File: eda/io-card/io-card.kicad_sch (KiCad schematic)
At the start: 22 parts, among them J3 PortA, J4 PortB, J5 ControlLines, J6 SPI, U1 W65C22SxP, U13 74HCT138, U2 W65C22SxP, U3 74HCT14, U5 74HCT00

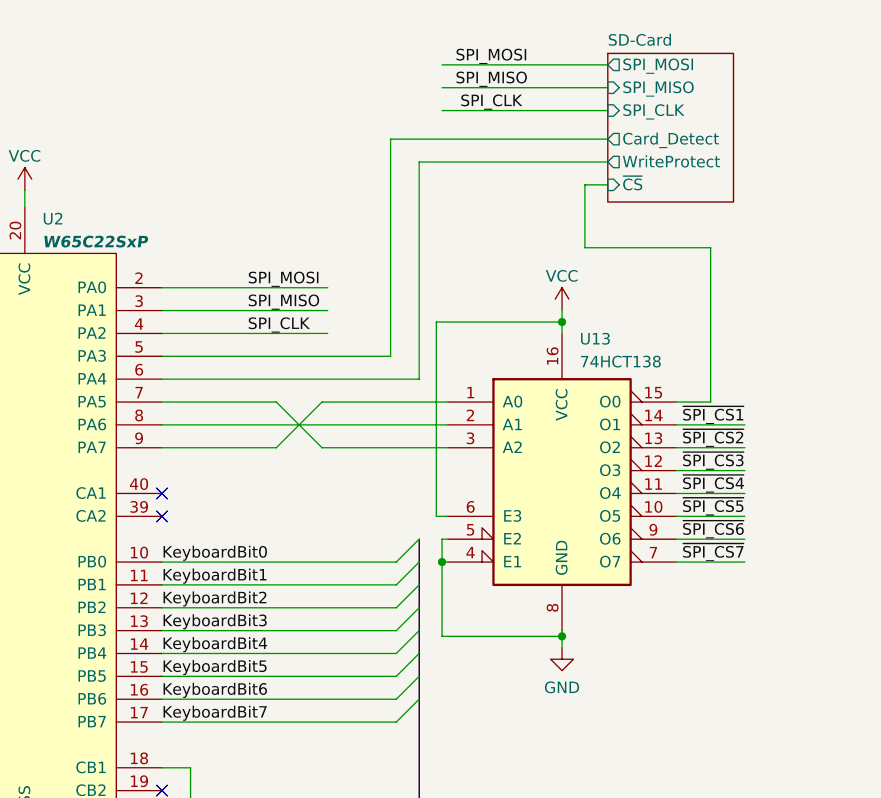
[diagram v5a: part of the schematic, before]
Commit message: Work on SPI with actual hardware
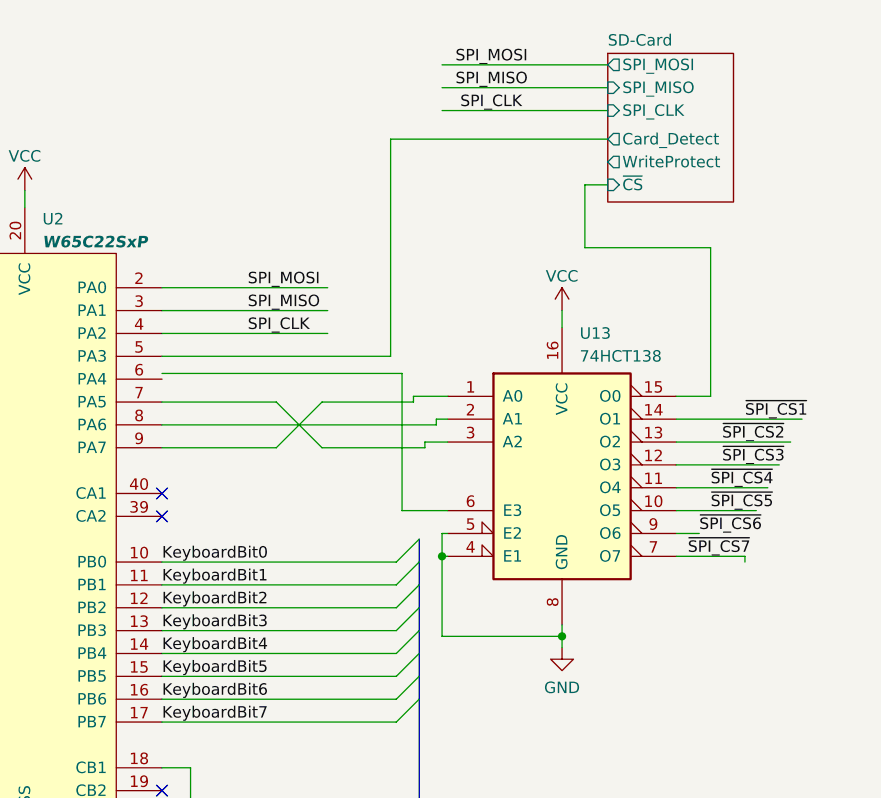
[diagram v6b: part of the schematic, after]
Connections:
- net SD-Card/WriteProtect: no longer U2.6 (PA4)
- net VCC: no longer U13.6 (E3)
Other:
- moved on the sheet: U13

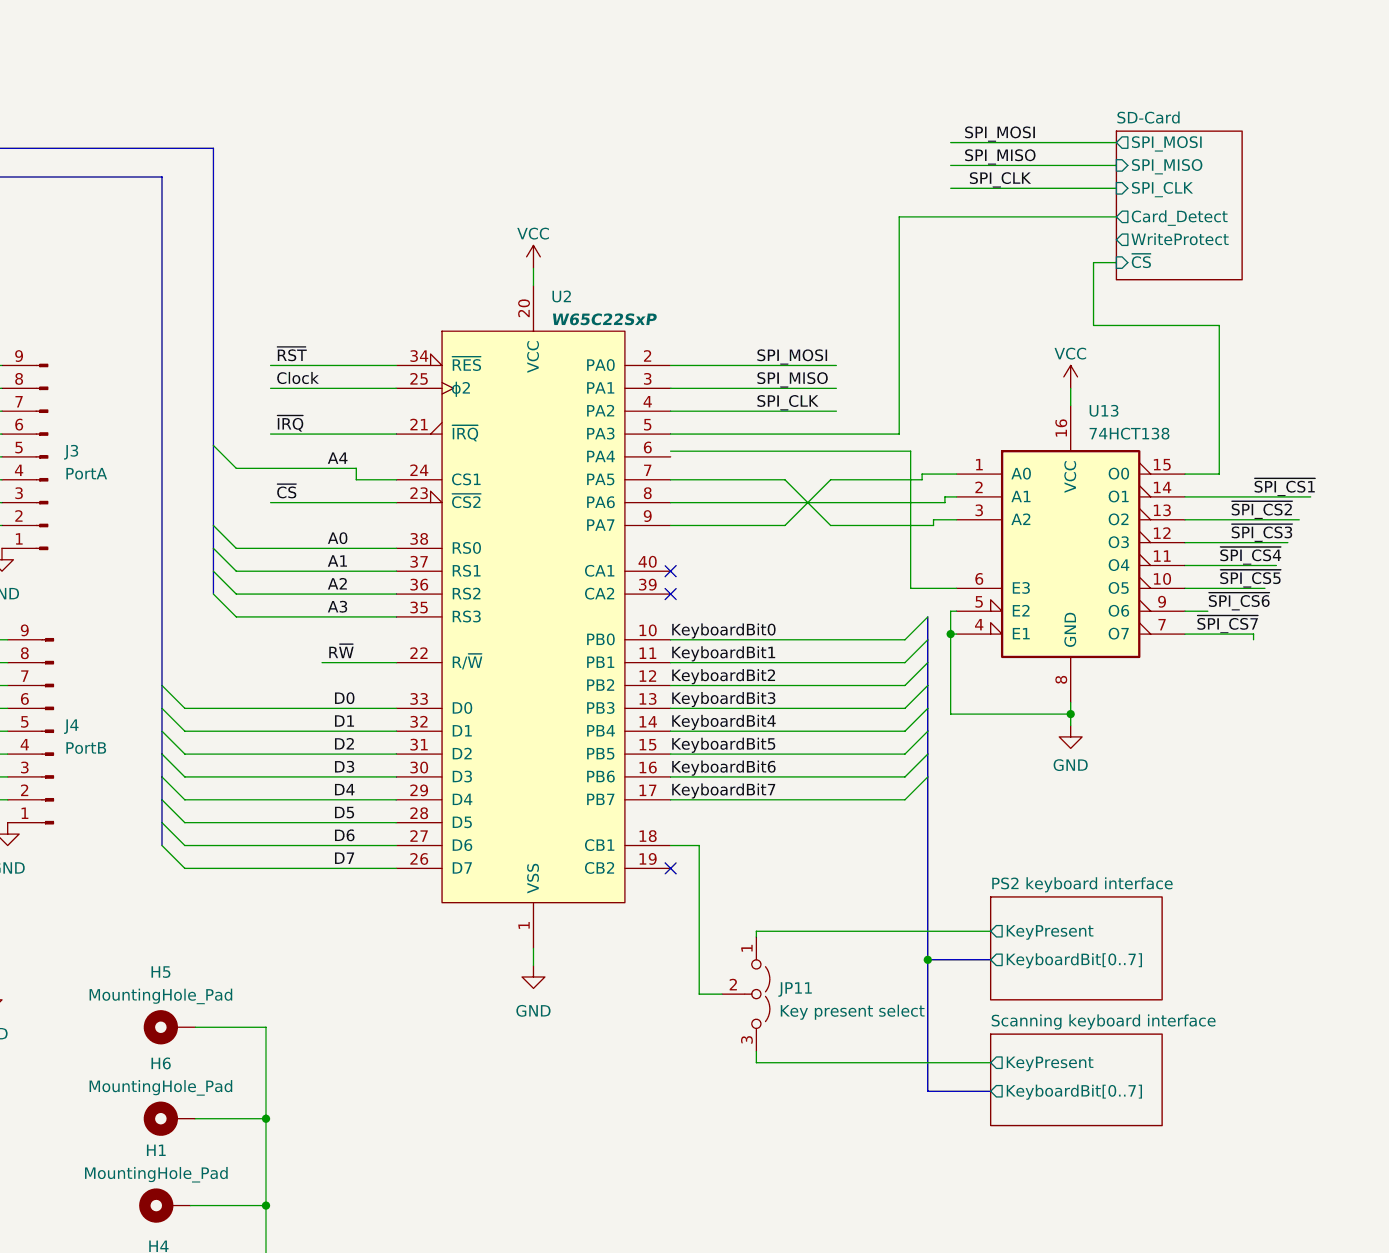
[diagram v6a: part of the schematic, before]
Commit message: Update simulator to match new io card via assignment
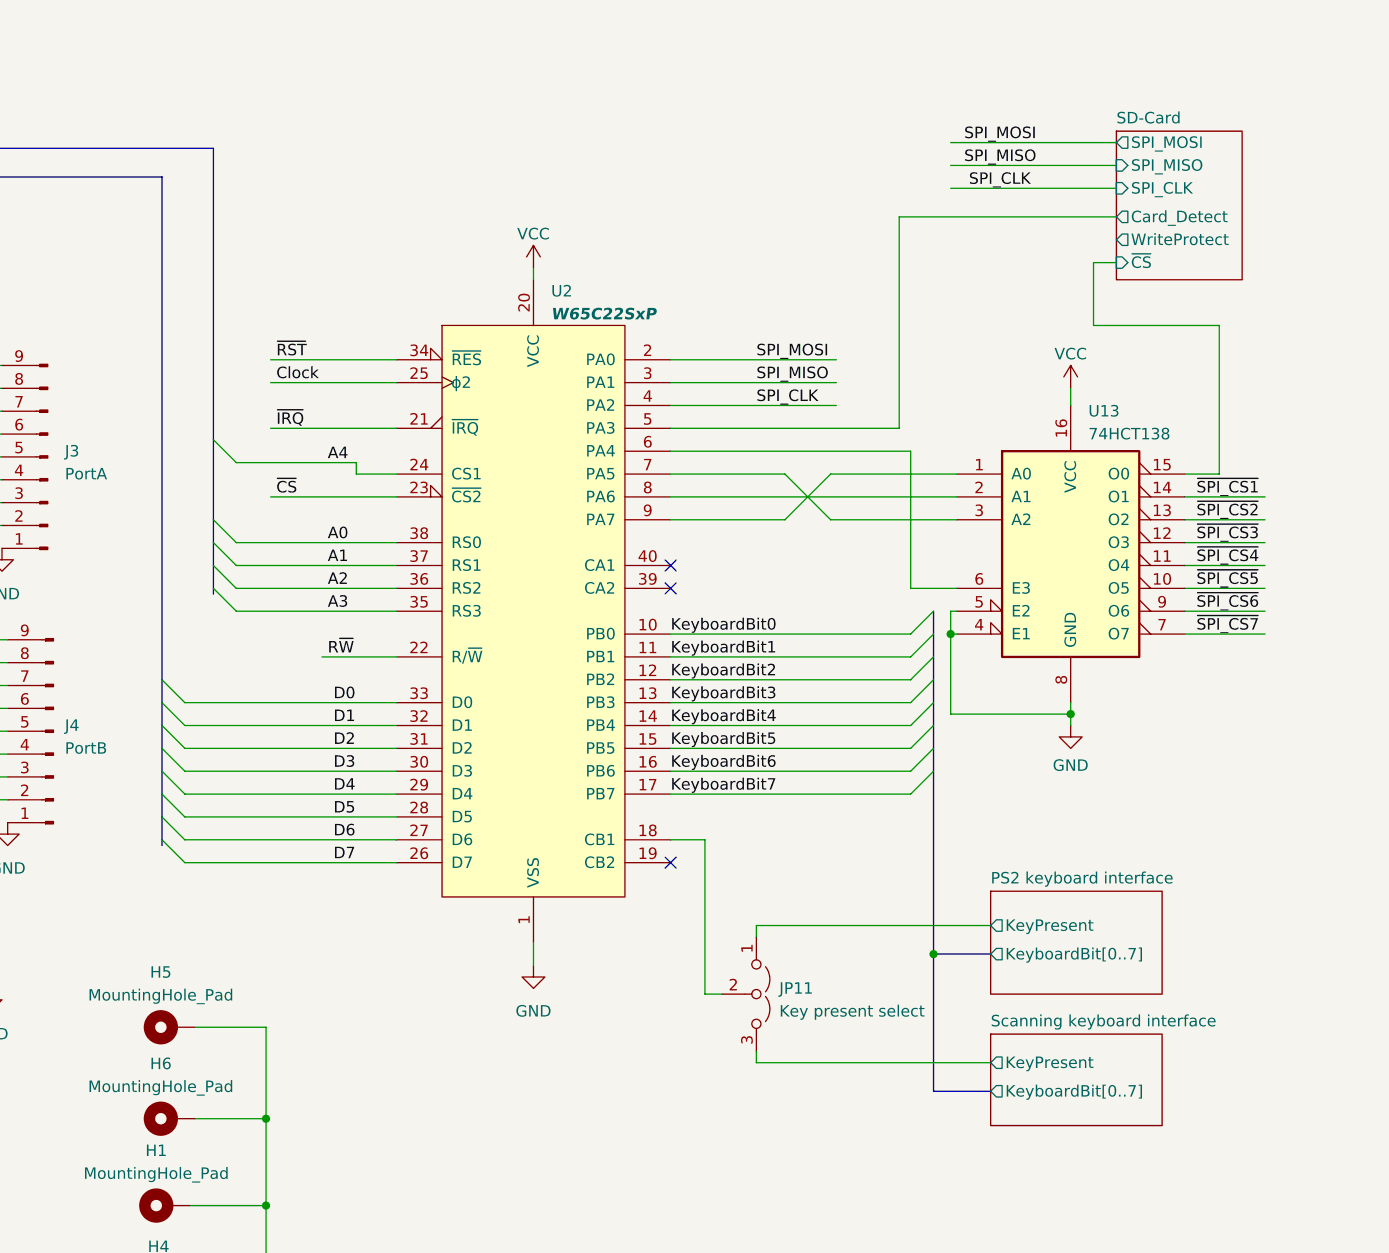
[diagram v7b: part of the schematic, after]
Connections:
- net at U2.6 (PA4): now also U13.6 (E3)
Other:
- moved on the sheet: U2

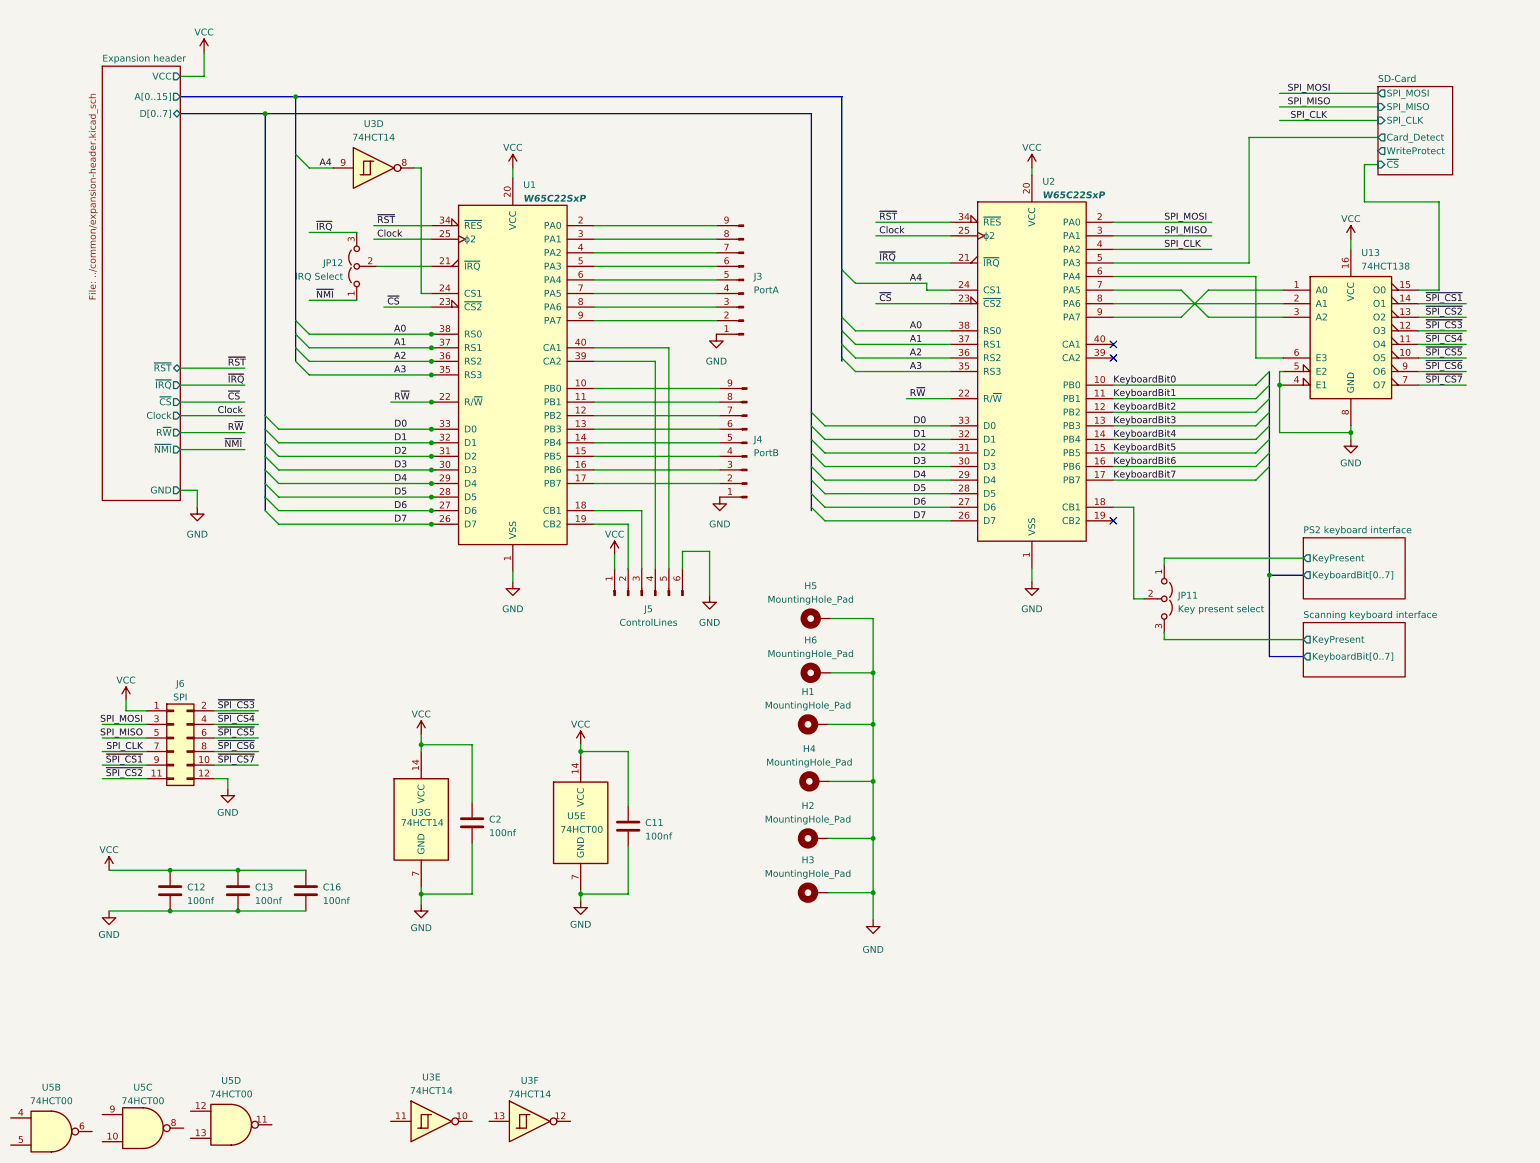
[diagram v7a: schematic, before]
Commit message: Add SPI
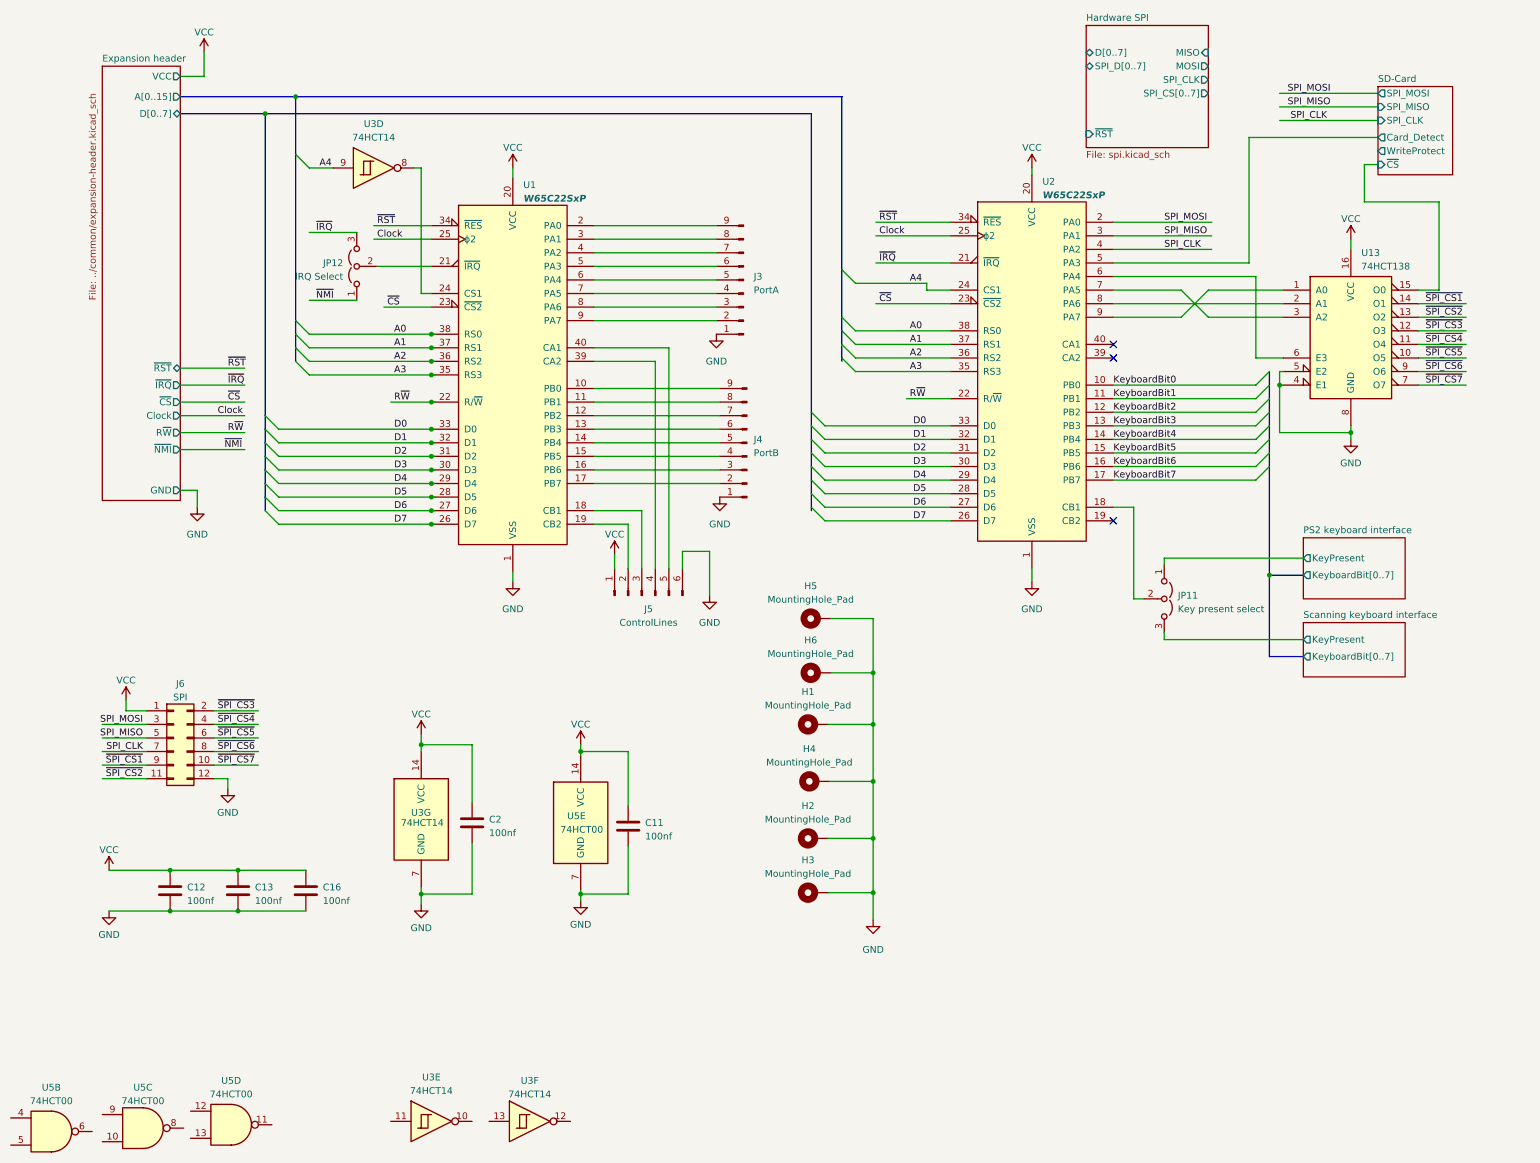
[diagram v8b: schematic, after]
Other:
- added sheet Hardware SPI (spi.kicad_sch)
